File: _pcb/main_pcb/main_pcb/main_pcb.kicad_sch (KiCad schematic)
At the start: 3 parts, among them J1 Conn_01x01_Pin, J2 Conn_01x01_Pin, U1 Pico

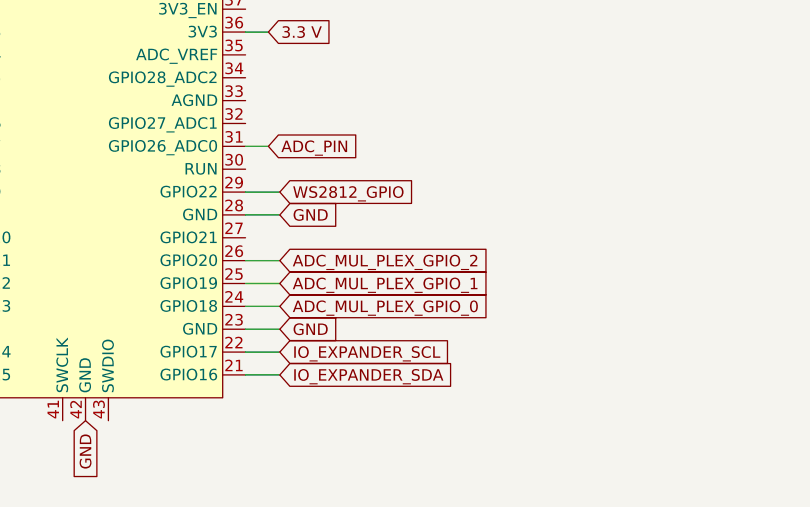
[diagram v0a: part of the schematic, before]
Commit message: position of pico not really clear
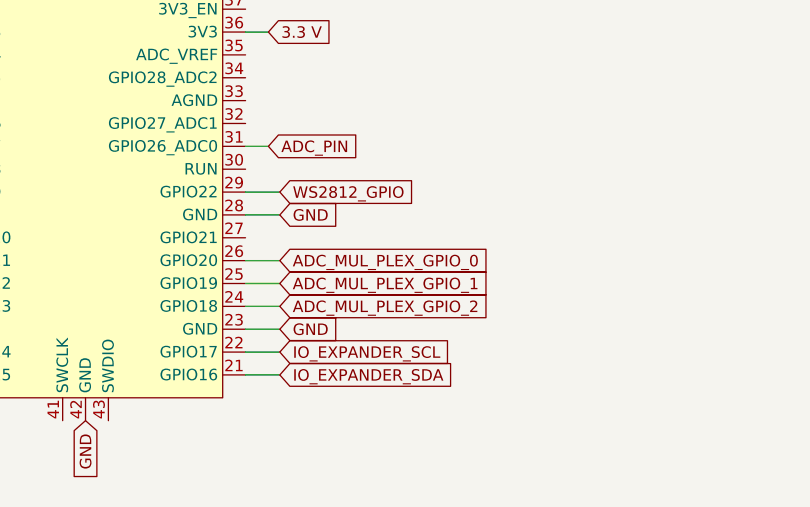
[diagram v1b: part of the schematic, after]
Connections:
- net ADC_MUL_PLEX_GPIO_0: now also U1.26 (GPIO20); no longer U1.24 (GPIO18)
- net ADC_MUL_PLEX_GPIO_2: now also U1.24 (GPIO18); no longer U1.26 (GPIO20)
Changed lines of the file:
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@@
 	(global_label "ADC_MUL_PLEX_GPIO_2"
 		(shape input)
-		(at 121.92 142.24 0)
+		(at 121.92 147.32 0)
 		(fields_autoplaced yes)
 		(effects
@@
 		)
 		(property "Intersheetrefs" "${INTERSHEET_REFS}"
-			(at 146.5556 142.24 0)
+			(at 146.5556 147.32 0)
 			(effects
 				(font
@@
 	(global_label "ADC_MUL_PLEX_GPIO_0"
 		(shape input)
-		(at 121.92 147.32 0)
+		(at 121.92 142.24 0)
 		(fields_autoplaced yes)
 		(effects
@@
 		)
 		(property "Intersheetrefs" "${INTERSHEET_REFS}"
-			(at 146.5556 147.32 0)
+			(at 146.5556 142.24 0)
 			(effects
 				(font

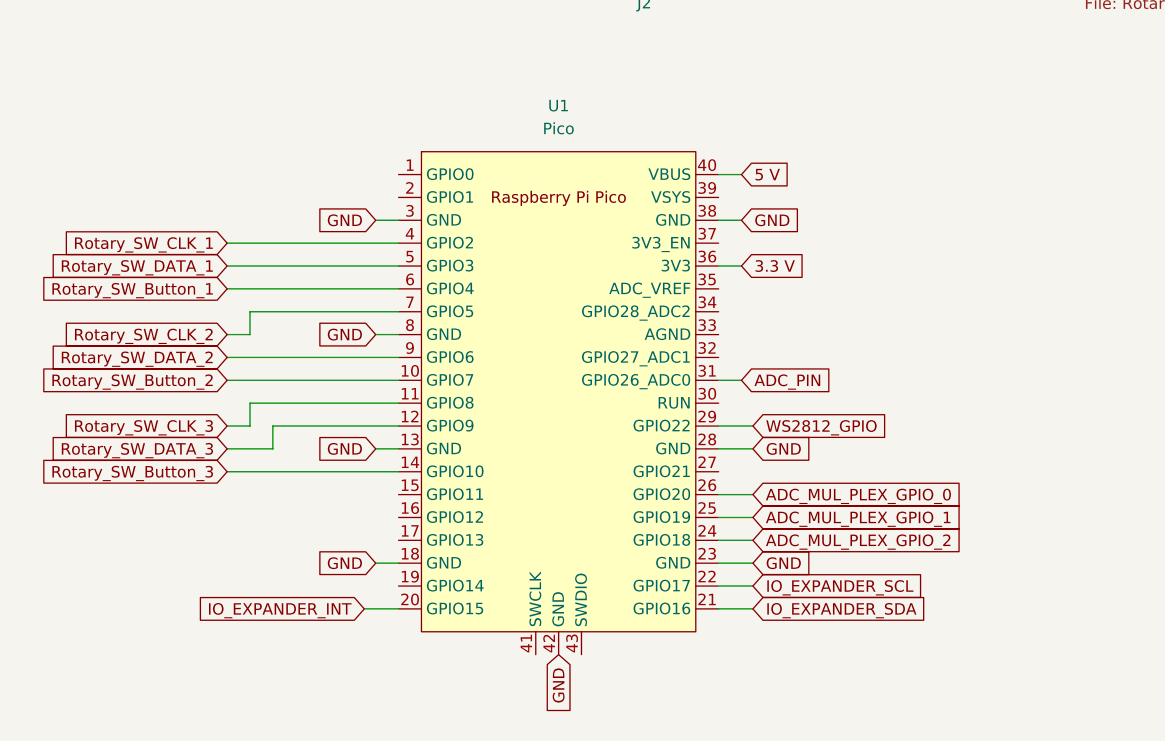
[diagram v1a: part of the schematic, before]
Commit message: changed the pins to fit possible hardware
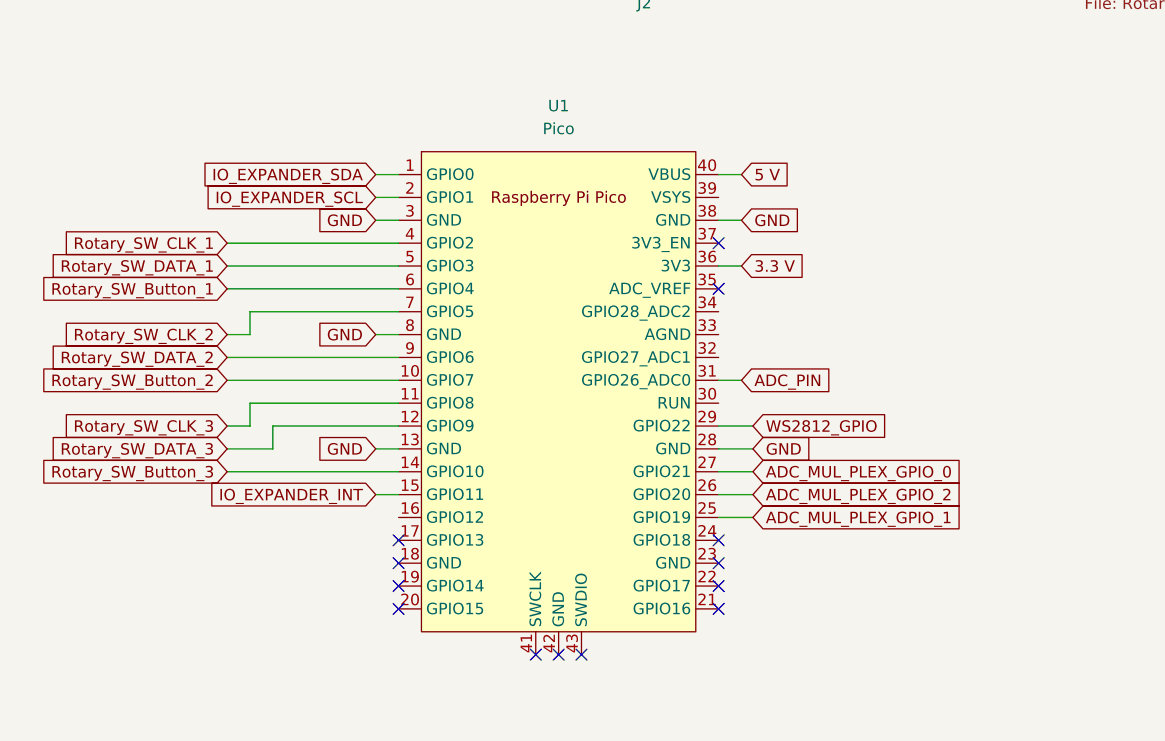
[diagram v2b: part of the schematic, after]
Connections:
- net ADC_MUL_PLEX_GPIO_0: now also U1.27 (GPIO21); no longer U1.26 (GPIO20)
- net ADC_MUL_PLEX_GPIO_2: now also U1.26 (GPIO20); no longer U1.24 (GPIO18)
- net GND: no longer U1.18 (GND), U1.23 (GND), U1.42 (GND)
- net IO_EXPANDER_INT: now also U1.15 (GPIO11); no longer U1.20 (GPIO15)
- net IO_EXPANDER_SCL: now also U1.2 (GPIO1); no longer U1.22 (GPIO17)
- net IO_EXPANDER_SDA: now also U1.1 (GPIO0); no longer U1.21 (GPIO16)
- no-connect marks 0 -> 13
